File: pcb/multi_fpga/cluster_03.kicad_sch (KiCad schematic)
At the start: 4 parts

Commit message: Fixed library and power issues.
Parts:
- A4: symbol CMOD_S7 -> multi_fpga:CMOD_S7
- C25, C26: symbol C -> multi_fpga:C
- VR1: symbol LDO_1V8 -> Regulator_Linear:MCP1700x-180xxTT
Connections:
- net +5V: no longer VR1.3 (IN)
- net C3_1V8: no longer VR1.2 (OUT)
- net GND: no longer VR1.1 (GND)
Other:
- moved on the sheet: VR1
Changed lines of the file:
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@@
 	)
 	(symbol
-		(lib_id "C")
+		(lib_id "multi_fpga:C")
 		(at 327.66 218.44 0)
 		(unit 1)
@@
 	)
 	(symbol
-		(lib_id "LDO_1V8")
+		(lib_id "Regulator_Linear:MCP1700x-180xxTT")
 		(at 300.99 218.44 0)
 		(unit 1)
@@
 	)
 	(symbol
-		(lib_id "power:C3_1V8")
+		(lib_id "multi_fpga:C3_1V8")
 		(at 269.24 214.63 0)
 		(unit 1)
@@
 	)
 	(symbol
-		(lib_id "power:C3_1V8")
+		(lib_id "multi_fpga:C3_1V8")
 		(at 327.66 214.63 0)
 		(unit 1)
@@
 	)
 	(symbol
-		(lib_id "CMOD_S7")
+		(lib_id "multi_fpga:CMOD_S7")
 		(at 262.89 142.24 0)
 		(unit 1)
@@
 	)
 	(symbol
-		(lib_id "C")
+		(lib_id "multi_fpga:C")
 		(at 252.73 218.44 0)
 		(unit 1)

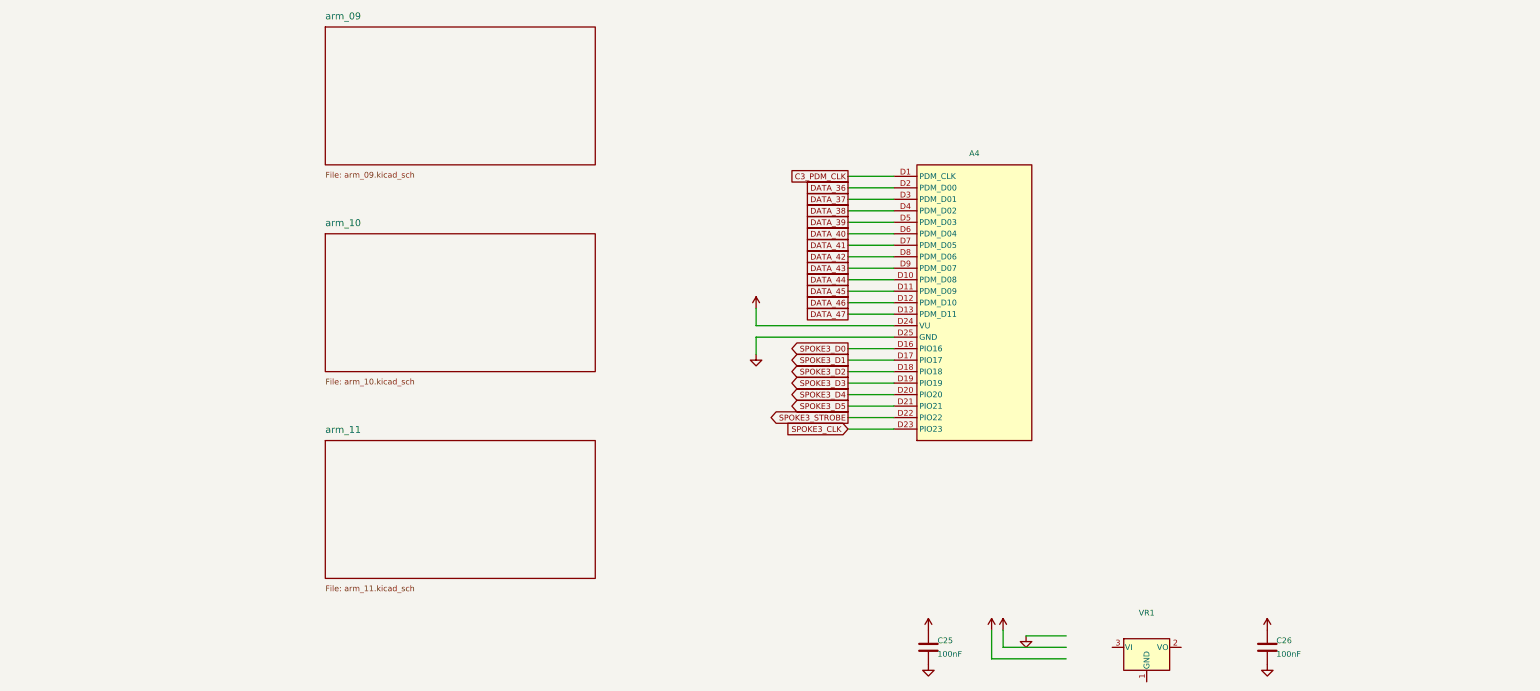
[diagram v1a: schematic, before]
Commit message: Fixed power and C ref des collisions.
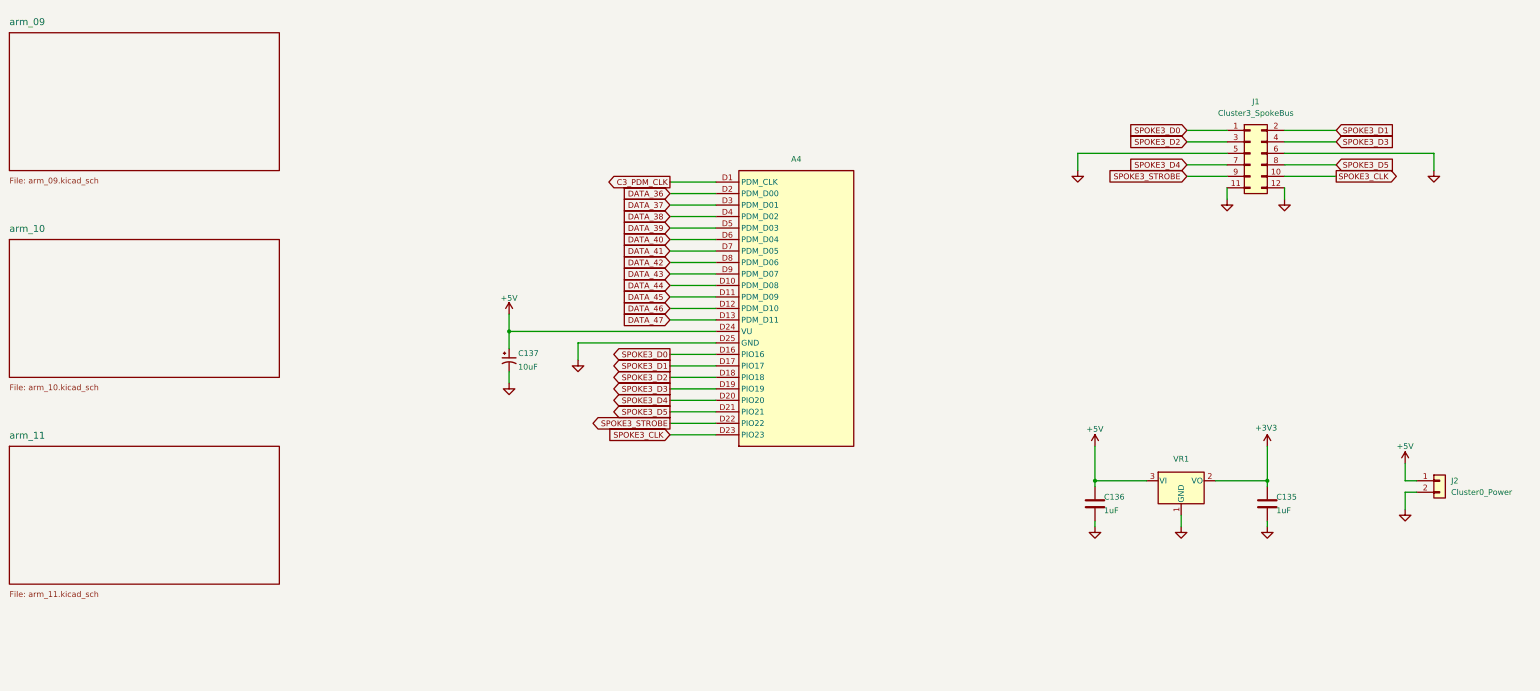
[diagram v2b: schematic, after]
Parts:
- removed C25, C26: 100nF, symbol multi_fpga:C
- added C135, C136: 1uF, Capacitor_SMD:C_0201_0603Metric, symbol multi_fpga:C
- added C137: 10uF, SparkFun-Capacitor:C_0603_1608Metric_Polar, symbol SparkFun-Capacitor:10uF_0603_6.3V_20%_Polar(Tant)
- added J1: Cluster3_SpokeBus, Connector_PinHeader_2.54mm:PinHeader_2x06_P2.54mm_Vertical, symbol Connector_Generic:Conn_02x06_Odd_Even
- added J2: Cluster0_Power, symbol Connector_Generic:Conn_01x02
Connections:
- net +5V: now also VR1.3 (VI), C136.1, C137.1, J2.1 (Pin_1)
- net GND: now also VR1.1 (GND), C135.2, C136.2, C137.2, J1.11 (Pin_11), J1.12 (Pin_12), J1.5 (Pin_5), J1.6 (Pin_6), J2.2 (Pin_2)
- net SPOKE3_CLK: now also J1.10 (Pin_10)
- net SPOKE3_D0: now also J1.1 (Pin_1)
- net SPOKE3_D1: now also J1.2 (Pin_2)
- net SPOKE3_D2: now also J1.3 (Pin_3)
- net SPOKE3_D3: now also J1.4 (Pin_4)
- net SPOKE3_D4: now also J1.7 (Pin_7)
- net SPOKE3_D5: now also J1.8 (Pin_8)
- net SPOKE3_STROBE: now also J1.9 (Pin_9)
- net +3V3: now reaches VR1.2 (VO)
- net +3V3: now also C135.1
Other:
- moved on the sheet: A4

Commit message: Fixed annotations.
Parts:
- renumbered J1 to J15, J2 to J16, VR1 to VR4
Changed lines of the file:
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@@
+				)
+			)
+			(project "top"
+				(path "/80f109c4-96c5-4385-bfb6-0f7a96b014ab/6d6a7308-a3f5-4ff9-b87f-6052e7b74f31"
+					(reference "C135")
+					(unit 1)
 				)
 			)
@@
 			(project "cluster_03"
 				(path "/663bb1a4-0642-453a-b4ab-859c751fcf14"
+					(reference "#PWR0736")
+					(unit 1)
+				)
+			)
+			(project "top"
+				(path "/80f109c4-96c5-4385-bfb6-0f7a96b014ab/6d6a7308-a3f5-4ff9-b87f-6052e7b74f31"
 					(reference "#PWR0736")
 					(unit 1)
@@
 				)
 			)
+			(project "top"
+				(path "/80f109c4-96c5-4385-bfb6-0f7a96b014ab/6d6a7308-a3f5-4ff9-b87f-6052e7b74f31"
+					(reference "#PWR0737")
+					(unit 1)
+				)
+			)
 		)
 	)
@@
 				)
 			)
+			(project "top"
+				(path "/80f109c4-96c5-4385-bfb6-0f7a96b014ab/6d6a7308-a3f5-4ff9-b87f-6052e7b74f31"
+					(reference "#PWR0738")
+					(unit 1)
+				)
+			)
 		)
 	)
@@
 				)
 			)
+			(project "top"
+				(path "/80f109c4-96c5-4385-bfb6-0f7a96b014ab/6d6a7308-a3f5-4ff9-b87f-6052e7b74f31"
+					(reference "#PWR0739")
+					(unit 1)
+				)
+			)
 		)
 	)
@@
 				)
 			)
+			(project "top"
+				(path "/80f109c4-96c5-4385-bfb6-0f7a96b014ab/6d6a7308-a3f5-4ff9-b87f-6052e7b74f31"
+					(reference "C136")
+					(unit 1)
+				)
+			)
 		)
 	)
@@
 				)
 			)
+			(project "top"
+				(path "/80f109c4-96c5-4385-bfb6-0f7a96b014ab/6d6a7308-a3f5-4ff9-b87f-6052e7b74f31"
+					(reference "#PWR0740")
+					(unit 1)
+				)
+			)
 		)
 	)
@@
 		(in_pos_files yes)
 		(dnp no)
-		(property "Reference" "VR1"
+		(property "Reference" "VR4"
 			(at 308.61 176.784 0)
 			(show_name no)
@@
 			(project "cluster_03"
 				(path "/663bb1a4-0642-453a-b4ab-859c751fcf14"
+					(reference "VR4")
+					(unit 1)
+				)
+			)
+			(project "top"
+				(path "/80f109c4-96c5-4385-bfb6-0f7a96b014ab/6d6a7308-a3f5-4ff9-b87f-6052e7b74f31"
 					(reference "VR1")
 					(unit 1)
@@
 				)
 			)
+			(project "top"
+				(path "/80f109c4-96c5-4385-bfb6-0f7a96b014ab/6d6a7308-a3f5-4ff9-b87f-6052e7b74f31"
+					(reference "#PWR0741")
+					(unit 1)
+				)
+			)
 		)
 	)
@@
 		(dnp no)
 		(fields_autoplaced yes)
-		(property "Reference" "J2"
+		(property "Reference" "J16"
 			(at 368.3 181.6099 0)
 			(show_name no)
@@
 			(project "cluster_03"
 				(path "/663bb1a4-0642-453a-b4ab-859c751fcf14"
+					(reference "J16")
+					(unit 1)
+				)
+			)
+			(project "top"
+				(path "/80f109c4-96c5-4385-bfb6-0f7a96b014ab/6d6a7308-a3f5-4ff9-b87f-6052e7b74f31"
 					(reference "J2")
 					(unit 1)
@@
 				)
 			)
+			(project "top"
+				(path "/80f109c4-96c5-4385-bfb6-0f7a96b014ab/6d6a7308-a3f5-4ff9-b87f-6052e7b74f31"
+					(reference "#PWR0742")
+					(unit 1)
+				)
+			)
 		)
 	)
@@
 			(project "cluster_03"
 				(path "/663bb1a4-0642-453a-b4ab-859c751fcf14"
+					(reference "#PWR0743")
+					(unit 1)
+				)
+			)
+			(project "top"
+				(path "/80f109c4-96c5-4385-bfb6-0f7a96b014ab/6d6a7308-a3f5-4ff9-b87f-6052e7b74f31"
 					(reference "#PWR0743")
 					(unit 1)
@@
 				)
 			)
+			(project "top"
+				(path "/80f109c4-96c5-4385-bfb6-0f7a96b014ab/6d6a7308-a3f5-4ff9-b87f-6052e7b74f31"
+					(reference "#PWR0744")
+					(unit 1)
+				)
+			)
 		)
 	)
@@
 				)
 			)
+			(project "top"
+				(path "/80f109c4-96c5-4385-bfb6-0f7a96b014ab/6d6a7308-a3f5-4ff9-b87f-6052e7b74f31"
+					(reference "#PWR0745")
+					(unit 1)
+				)
+			)
 		)
 	)
@@
 				)
 			)
+			(project "top"
+				(path "/80f109c4-96c5-4385-bfb6-0f7a96b014ab/6d6a7308-a3f5-4ff9-b87f-6052e7b74f31"
+					(reference "#PWR0746")
+					(unit 1)
+				)
+			)
 		)
 	)
@@
 		(dnp no)
 		(fields_autoplaced yes)
-		(property "Reference" "J1"
+		(property "Reference" "J15"
 			(at 325.12 97.79 0)
 			(show_name no)
@@
 			(project "cluster_03"
 				(path "/663bb1a4-0642-453a-b4ab-859c751fcf14"
+					(reference "J15")
+					(unit 1)
+				)
+			)
+			(project "top"
+				(path "/80f109c4-96c5-4385-bfb6-0f7a96b014ab/6d6a7308-a3f5-4ff9-b87f-6052e7b74f31"
 					(reference "J1")
 					(unit 1)
@@
 			(project "cluster_03"
 				(path "/663bb1a4-0642-453a-b4ab-859c751fcf14"
+					(reference "#PWR0747")
+					(unit 1)
+				)
+			)
+			(project "top"
+				(path "/80f109c4-96c5-4385-bfb6-0f7a96b014ab/6d6a7308-a3f5-4ff9-b87f-6052e7b74f31"
 					(reference "#PWR0747")
 					(unit 1)
@@
 				)
 			)
+			(project "top"
+				(path "/80f109c4-96c5-4385-bfb6-0f7a96b014ab/6d6a7308-a3f5-4ff9-b87f-6052e7b74f31"
+					(reference "#PWR0748")
+					(unit 1)
+				)
+			)
 		)
 	)
@@
 				)
 			)
+			(project "top"
+				(path "/80f109c4-96c5-4385-bfb6-0f7a96b014ab/6d6a7308-a3f5-4ff9-b87f-6052e7b74f31"
+					(reference "C137")
+					(unit 1)
+				)
+			)
 		)
 	)
@@
 					(reference "#PWR0749")
 					(unit 1)
+				)
+			)
+			(project "top"
+				(path "/80f109c4-96c5-4385-bfb6-0f7a96b014ab/6d6a7308-a3f5-4ff9-b87f-6052e7b74f31"
+					(reference "#PWR0749")
+					(unit 1)

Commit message: Fixed annotation issues.
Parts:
- renumbered J15 to J1, J16 to J2, VR4 to VR1
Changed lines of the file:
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@@
 		(in_pos_files yes)
 		(dnp no)
-		(property "Reference" "VR4"
+		(property "Reference" "VR1"
 			(at 308.61 176.784 0)
 			(show_name no)
@@
 		(dnp no)
 		(fields_autoplaced yes)
-		(property "Reference" "J16"
+		(property "Reference" "J2"
 			(at 368.3 181.6099 0)
 			(show_name no)
@@
 		(dnp no)
 		(fields_autoplaced yes)
-		(property "Reference" "J15"
+		(property "Reference" "J1"
 			(at 325.12 97.79 0)
 			(show_name no)
@@
 		)
 	)
-	(embedded_fonts no)
 )

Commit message: Fixed regulator connection errors and dangling wire.
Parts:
- J16: renamed from J2; value Cluster0_Power -> Cluster3_Power
- renumbered J1 to J15, VR1 to VR4
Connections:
- net +3V3 renamed C3_1V8
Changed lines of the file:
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@@
 	)
 	(symbol
-		(lib_id "power:+3V3")
+		(lib_id "multi_fpga:C3_1V8")
 		(at 327.66 173.99 0)
 		(unit 1)
@@
 			)
 		)
-		(property "Value" "+3V3"
+		(property "Value" "C3_1V8"
 			(at 327.406 169.926 0)
 			(show_name no)
@@
 		(in_pos_files yes)
 		(dnp no)
-		(property "Reference" "VR1"
+		(property "Reference" "VR4"
 			(at 308.61 176.784 0)
 			(show_name no)
@@
 		(dnp no)
 		(fields_autoplaced yes)
-		(property "Reference" "J2"
+		(property "Reference" "J16"
 			(at 368.3 181.6099 0)
 			(show_name no)
@@
 			)
 		)
-		(property "Value" "Cluster0_Power"
+		(property "Value" "Cluster3_Power"
 			(at 368.3 184.1499 0)
 			(show_name no)
@@
 		(dnp no)
 		(fields_autoplaced yes)
-		(property "Reference" "J1"
+		(property "Reference" "J15"
 			(at 325.12 97.79 0)
 			(show_name no)
@@
 		)
 	)
+	(embedded_fonts no)
 )

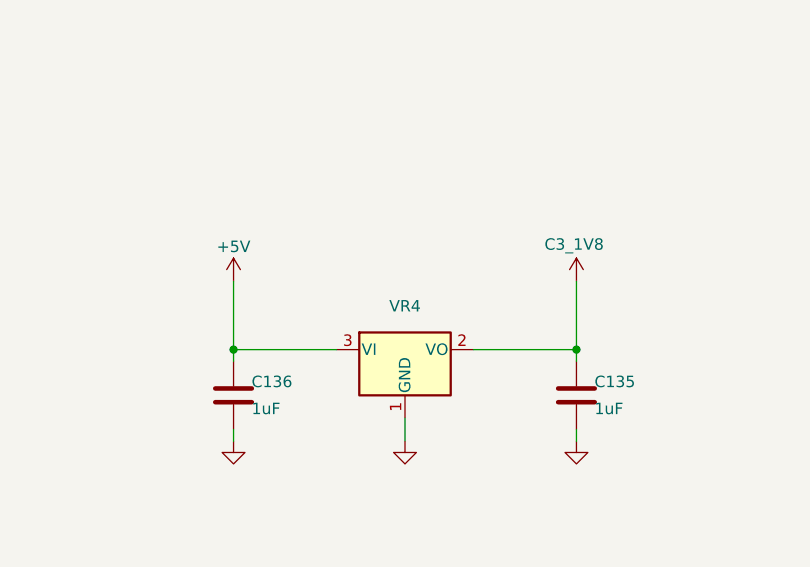
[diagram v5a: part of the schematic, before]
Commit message: Added the LDO regulator part numbers.
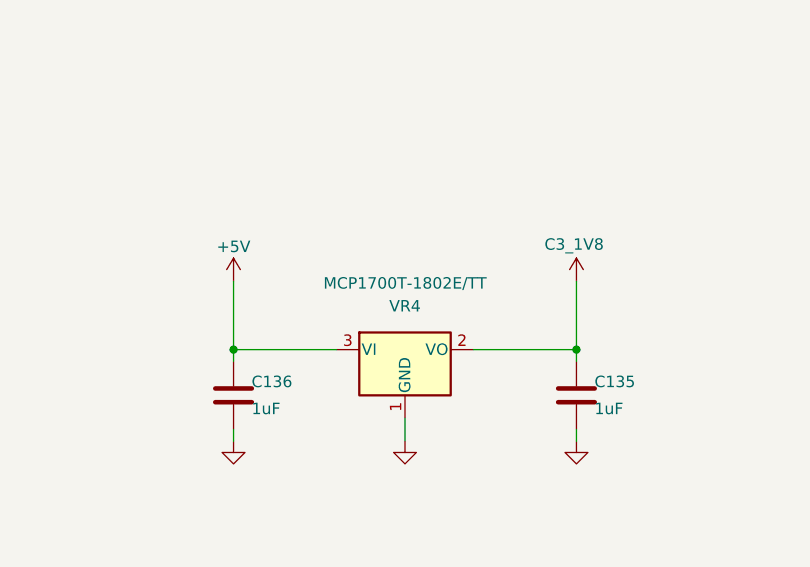
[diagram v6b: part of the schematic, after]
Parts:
- VR4: value (none) -> MCP1700T-1802E/TT
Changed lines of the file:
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@@
 			)
 		)
-		(property "Value" ""
-			(at 308.61 181.61 0)
+		(property "Value" "MCP1700T-1802E/TT"
+			(at 308.61 174.244 0)
 			(show_name no)
 			(do_not_autoplace no)

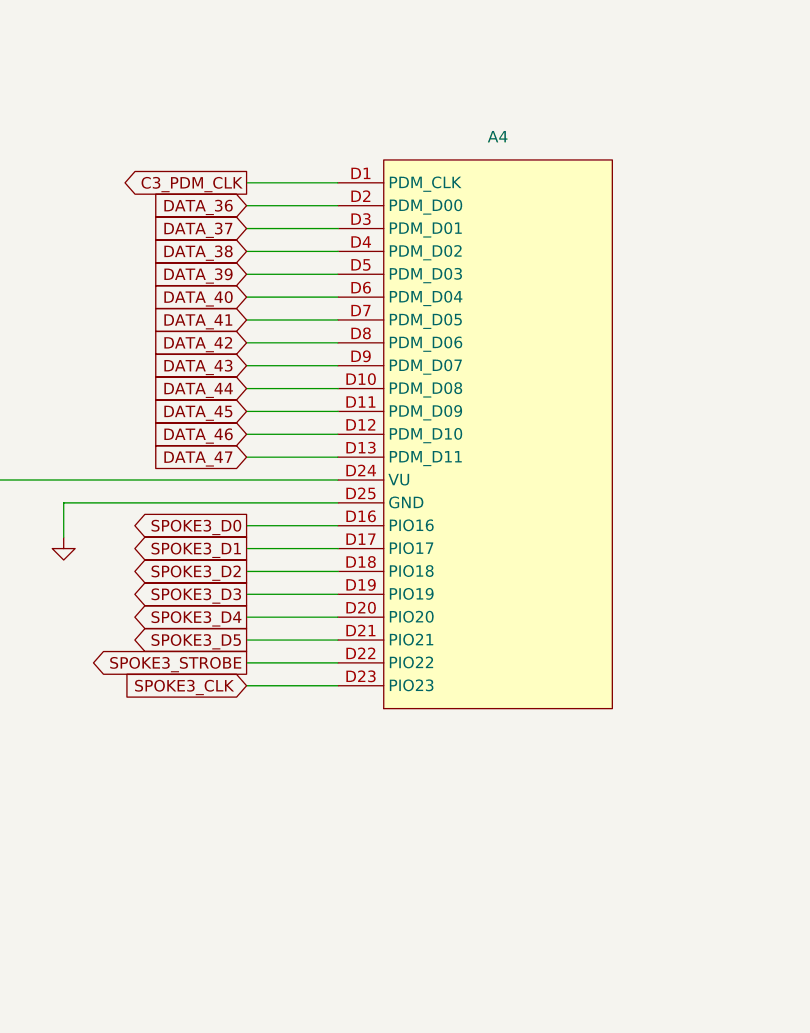
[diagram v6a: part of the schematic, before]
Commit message: Fixed FPGA module symbols.
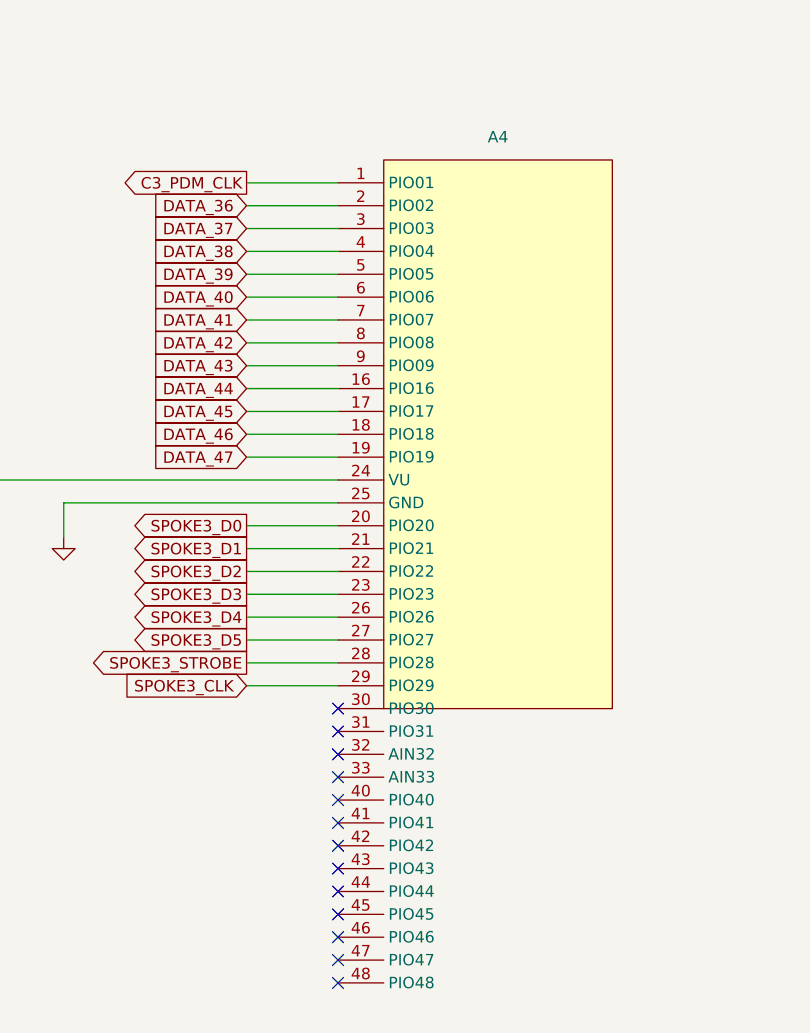
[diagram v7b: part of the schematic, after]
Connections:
- net +5V: now also A4.24 (VU); no longer A4.D24 (VU)
- net C3_PDM_CLK: now also A4.1 (PIO01); no longer A4.D1 (PDM_CLK)
- net DATA_36: now also A4.2 (PIO02); no longer A4.D2 (PDM_D00)
- net DATA_37: now also A4.3 (PIO03); no longer A4.D3 (PDM_D01)
- net DATA_38: now also A4.4 (PIO04); no longer A4.D4 (PDM_D02)
- net DATA_39: now also A4.5 (PIO05); no longer A4.D5 (PDM_D03)
- net DATA_40: now also A4.6 (PIO06); no longer A4.D6 (PDM_D04)
- net DATA_41: now also A4.7 (PIO07); no longer A4.D7 (PDM_D05)
- net DATA_42: now also A4.8 (PIO08); no longer A4.D8 (PDM_D06)
- net DATA_43: now also A4.9 (PIO09); no longer A4.D9 (PDM_D07)
- net DATA_44: now also A4.16 (PIO16); no longer A4.D10 (PDM_D08)
- net DATA_45: now also A4.17 (PIO17); no longer A4.D11 (PDM_D09)
- net DATA_46: now also A4.18 (PIO18); no longer A4.D12 (PDM_D10)
- net DATA_47: now also A4.19 (PIO19); no longer A4.D13 (PDM_D11)
- net GND: now also A4.25 (GND); no longer A4.D25 (GND)
- net SPOKE3_CLK: now also A4.29 (PIO29); no longer A4.D23 (PIO23)
- net SPOKE3_D0: now also A4.20 (PIO20); no longer A4.D16 (PIO16)
- net SPOKE3_D1: now also A4.21 (PIO21); no longer A4.D17 (PIO17)
- net SPOKE3_D2: now also A4.22 (PIO22); no longer A4.D18 (PIO18)
- net SPOKE3_D3: now also A4.23 (PIO23); no longer A4.D19 (PIO19)
- net SPOKE3_D4: now also A4.26 (PIO26); no longer A4.D20 (PIO20)
- net SPOKE3_D5: now also A4.27 (PIO27); no longer A4.D21 (PIO21)
- net SPOKE3_STROBE: now also A4.28 (PIO28); no longer A4.D22 (PIO22)
- no-connect marks 0 -> 13
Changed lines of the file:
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@@
 	)
 	(embedded_fonts no)
+	(no_connect
+		(at 205.74 173.99)
+	)
+	(no_connect
+		(at 205.74 176.53)
+	)
+	(no_connect
+		(at 205.74 179.07)
+	)
+	(no_connect
+		(at 205.74 181.61)
+	)
+	(no_connect
+		(at 205.74 184.15)
+	)
+	(no_connect
+		(at 205.74 186.69)
+	)
+	(no_connect
+		(at 205.74 189.23)
+	)
+	(no_connect
+		(at 205.74 191.77)
+	)
+	(no_connect
+		(at 205.74 194.31)
+	)
+	(no_connect
+		(at 205.74 196.85)
+	)
+	(no_connect
+		(at 205.74 199.39)
+	)
+	(no_connect
+		(at 205.74 201.93)
+	)
+	(no_connect
+		(at 205.74 204.47)
+	)
 )
